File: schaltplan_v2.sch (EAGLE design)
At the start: 18 parts

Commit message: layout/board redesign
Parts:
- removed D10, D3, D4, D5, D6, D7, D8, D9: 1N4004, diode:1N4004
- removed U$3, U$4, U$5: JS_05_MN_KT, n39:JS_05_MN_KT
- removed U$6, U$7, U$8: JS_05_N_K, n39:JS_05_N_K
- added T1, T2: 2N3565, transistor:2N3565
- added X1: SSW-102-02-S-S-RA, con-samtec:SSW-102-02-S-S-RA
- added X3: SSW-103-02-S-S-RA, con-samtec:SSW-103-02-S-S-RA
- added X4: SSW-109-02-S-S-RA, con-samtec:SSW-109-02-S-S-RA
- U$1: value JS_05_N_K -> JS_05_MN_KT; device n39:JS_05_N_K -> n39:JS_05_MN_KT
- U$2: value JS_05_MN_KT -> JS_05_N_K; device n39:JS_05_MN_KT -> n39:JS_05_N_K
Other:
- moved on the sheet: D1, D2
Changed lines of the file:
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@@
 <parts>
 <part name="D1" library="diode" deviceset="1N4004" device=""/>
+<part name="U$1" library="n39" deviceset="JS_05_MN_KT" device=""/>
+<part name="U$2" library="n39" deviceset="JS_05_N_K" device=""/>
+<part name="T1" library="transistor" deviceset="2N3565" device=""/>
+<part name="R1" library="docu-dummy" deviceset="R" device=""/>
 <part name="D2" library="diode" deviceset="1N4004" device=""/>
-<part name="U$1" library="n39" deviceset="JS_05_N_K" device=""/>
-<part name="U$2" library="n39" deviceset="JS_05_MN_KT" device=""/>
-<part name="U$3" library="n39" deviceset="JS_05_MN_KT" device=""/>
-<part name="U$4" library="n39" deviceset="JS_05_MN_KT" device=""/>
-<part name="U$5" library="n39" deviceset="JS_05_MN_KT" device=""/>
-<part name="U$6" library="n39" deviceset="JS_05_N_K" device=""/>
-<part name="U$7" library="n39" deviceset="JS_05_N_K" device=""/>
-<part name="U$8" library="n39" deviceset="JS_05_N_K" device=""/>
-<part name="D3" library="diode" deviceset="1N4004" device=""/>
-<part name="D4" library="diode" deviceset="1N4004" device=""/>
-<part name="D5" library="diode" deviceset="1N4004" device=""/>
-<part name="D6" library="diode" deviceset="1N4004" device=""/>
-<part name="D7" library="diode" deviceset="1N4004" device=""/>
-<part name="D8" library="diode" deviceset="1N4004" device=""/>
-<part name="D9" library="diode" deviceset="1N4004" device=""/>
-<part name="D10" library="diode" deviceset="1N4004" device=""/>
+<part name="T2" library="transistor" deviceset="2N3565" device=""/>
+<part name="R2" library="docu-dummy" deviceset="R" device=""/>
+<part name="X1" library="con-samtec" deviceset="SSW-102-02-S-S" device="-RA"/>
+<part name="X3" library="con-samtec" deviceset="SSW-103-02-S-S" device="-RA"/>
+<part name="X4" library="con-samtec" deviceset="SSW-109-02-S-S" device="-RA"/>
 </parts>
 <sheets>
@@
 </plain>
 <instances>
-<instance part="D1" gate="1" x="38.1" y="58.42" rot="R90"/>
-<instance part="D2" gate="1" x="38.1" y="38.1" rot="R90"/>
-<instance part="U$1" gate="G$1" x="96.52" y="20.32"/>
-<instance part="U$2" gate="G$1" x="53.34" y="48.26"/>
-<instance part="U$3" gate="G$1" x="96.52" y="48.26"/>
-<instance part="U$4" gate="G$1" x="134.62" y="48.26"/>
-<instance part="U$5" gate="G$1" x="134.62" y="30.48"/>
-<instance part="U$6" gate="G$1" x="96.52" y="2.54"/>
-<instance part="U$7" gate="G$1" x="137.16" y="20.32"/>
-<instance part="U$8" gate="G$1" x="137.16" y="2.54"/>
-<instance part="D3" gate="1" x="38.1" y="27.94" rot="R90"/>
-<instance part="D4" gate="1" x="38.1" y="20.32" rot="R90"/>
-<instance part="D5" gate="1" x="33.02" y="27.94" rot="R90"/>
-<instance part="D6" gate="1" x="33.02" y="38.1" rot="R90"/>
-<instance part="D7" gate="1" x="33.02" y="58.42" rot="R90"/>
-<instance part="D8" gate="1" x="22.86" y="30.48" rot="R90"/>
-<instance part="D9" gate="1" x="25.4" y="45.72" rot="R90"/>
-<instance part="D10" gate="1" x="33.02" y="20.32" rot="R90"/>
+<instance part="D1" gate="1" x="71.12" y="53.34"/>
+<instance part="U$1" gate="G$1" x="93.98" y="45.72"/>
+<instance part="U$2" gate="G$1" x="93.98" y="20.32"/>
+<instance part="T1" gate="G$1" x="60.96" y="48.26"/>
+<instance part="R1" gate="G$1" x="50.8" y="48.26"/>
+<instance part="D2" gate="1" x="71.12" y="27.94"/>
+<instance part="T2" gate="G$1" x="60.96" y="22.86"/>
+<instance part="R2" gate="G$1" x="50.8" y="22.86"/>
+<instance part="X1" gate="-1" x="38.1" y="71.12"/>
+<instance part="X1" gate="-2" x="38.1" y="68.58"/>
+<instance part="X3" gate="-1" x="121.92" y="68.58" rot="R180"/>
+<instance part="X3" gate="-2" x="121.92" y="71.12" rot="R180"/>
+<instance part="X3" gate="-3" x="121.92" y="73.66" rot="R180"/>
+<instance part="X4" gate="-1" x="17.78" y="48.26"/>
+<instance part="X4" gate="-2" x="17.78" y="45.72"/>
+<instance part="X4" gate="-3" x="17.78" y="43.18"/>
+<instance part="X4" gate="-4" x="17.78" y="40.64"/>
+<instance part="X4" gate="-5" x="17.78" y="38.1"/>
+<instance part="X4" gate="-6" x="17.78" y="35.56"/>
+<instance part="X4" gate="-7" x="17.78" y="33.02"/>
+<instance part="X4" gate="-8" x="17.78" y="30.48"/>
+<instance part="X4" gate="-9" x="17.78" y="27.94"/>
 </instances>
 <busses>

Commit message: schaltplan_v2 finalized
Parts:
- added C1: (no value), rcl:CPOL-EUE3.5-8
- added C2: (no value), rcl:C-EU025-030X050
- added D10, D3, D4, D5, D6, D7, D8, D9: 1N4004, diode:1N4004
- added R1, R2, R3, R4, R5, R6, R7, R8: (no value), resistor:R-EU_0204/2V
- added T3, T4, T5, T6, T7, T8: 2N3565, transistor:2N3565
- added U$3, U$5, U$7: JS_05_MN_KT, n39:JS_05_MN_KT
- added U$4, U$6, U$8: JS_05_N_K, n39:JS_05_N_K
- added X2: SSW-102-02-S-S-RA, con-samtec:SSW-102-02-S-S-RA
- added X5, X6, X7: SSW-103-02-S-S-RA, con-samtec:SSW-103-02-S-S-RA
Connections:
- new net N$1: X2-1.1, X3-1.1, X5-1.1, X6-1.1, X7-1.1
- new net N$10: C1.-, C2.2, D10.A, T1.C, T2.C, T3.C, T4.C, T5.C, T6.C, T7.C, T8.C, X4-1.1
- new net N$11: R2.1, X4-3.1
- new net N$12: D2.A, T2.E, U$2.P$1
- new net N$13: R6.2, T6.B
- new net N$14: R3.1, X4-4.1
- new net N$16: U$4.P$5, X5-2.1
- new net N$17: U$4.P$4, X5-3.1
- new net N$18: U$3.P$4, U$4.P$3
- new net N$2: U$2.P$5, X3-2.1
- new net N$20: D3.A, T3.E, U$3.P$1
- new net N$21: C1.+, C2.1, D1.C, D2.C, D3.C, D4.C, D5.C, D6.C, D7.C, D8.C, D9.C, U$1.P$2, U$2.P$2, U$3.P$2, U$4.P$2, U$5.P$2, U$6.P$2, U$7.P$2, U$8.P$2
- new net N$22: R3.2, T3.B
- new net N$23: R4.1, X4-5.1
- new net N$25: D4.A, T4.E, U$4.P$1
- new net N$26: R5.1, X4-6.1
- new net N$27: R2.2, T2.B
- new net N$28: R4.2, T4.B
- new net N$3: U$2.P$4, X3-3.1
- new net N$30: U$6.P$5, X6-2.1
- new net N$31: U$6.P$4, X6-3.1
- new net N$32: U$5.P$4, U$6.P$3
- new net N$34: D5.A, T5.E, U$5.P$1
- new net N$36: R5.2, T5.B
- new net N$37: R6.1, X4-7.1
- new net N$39: D6.A, T6.E, U$6.P$1
- new net N$4: U$1.P$4, U$2.P$3
- new net N$40: R8.2, T8.B
- new net N$42: U$8.P$5, X7-2.1
- new net N$43: U$8.P$4, X7-3.1
- new net N$44: U$7.P$4, U$8.P$3
- new net N$46: D7.A, T7.E, U$7.P$1
- new net N$48: R7.2, T7.B
- new net N$49: R7.1, X4-8.1
- new net N$5: U$1.P$3, U$3.P$3, U$5.P$3, U$7.P$3, X2-2.1
- new net N$51: D8.A, T8.E, U$8.P$1
- new net N$53: D9.A, X1-1.1
- new net N$54: D10.C, X1-2.1
- new net N$6: D1.A, T1.E, U$1.P$1
- new net N$7: R8.1, X4-9.1
- new net N$8: R1.2, T1.B
- new net N$9: R1.1, X4-2.1
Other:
- moved on the sheet: X1-1, X1-2, X3-1, X3-2, X3-3

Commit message: more fixes
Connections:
- removed net N$10: C1.-, C2.2, D10.A, T1.C, T2.C, T3.C, T4.C, T5.C, T6.C, T7.C, T8.C, X4-1.1
- removed net N$21: C1.+, C2.1, D1.C, D2.C, D3.C, D4.C, D5.C, D6.C, D7.C, D8.C, D9.C, U$1.P$2, U$2.P$2, U$3.P$2, U$4.P$2, U$5.P$2, U$6.P$2, U$7.P$2, U$8.P$2
- removed net N$53: D9.A, X1-1.1
- removed net N$54: D10.C, X1-2.1
- new net N$15: D9.C, X1-1.1
- new net N$19: D10.A, X1-2.1
- new net N$24: C1.+, C2.2, D10.C, T1.C, T2.C, T3.C, T4.C, T5.C, T6.C, T7.C, T8.C, X4-1.1
- new net N$29: C1.-, C2.1, D1.C, D2.C, D3.C, D4.C, D5.C, D6.C, D7.C, D8.C, D9.A, U$1.P$2, U$2.P$2, U$3.P$2, U$4.P$2, U$5.P$2, U$6.P$2, U$7.P$2, U$8.P$2
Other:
- moved on the sheet: C1, D10, D9

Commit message: more fixes
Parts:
- removed X4: SSW-109-02-S-S-RA, con-samtec:SSW-109-02-S-S-RA
- added X8: SSW-110-02-S-S-RA, con-samtec:SSW-110-02-S-S-RA
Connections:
- removed net N$29 (its old number): C1.-, C2.1, D1.C, D2.C, D3.C, D4.C, D5.C, D6.C, D7.C, D8.C, D9.A, U$1.P$2, U$2.P$2, U$3.P$2, U$4.P$2, U$5.P$2, U$6.P$2, U$7.P$2, U$8.P$2
- new net N$19: C1.-, C2.1, D9.A, T1.C, T2.C, T3.C, T4.C, T5.C, T6.C, T7.C, T8.C, X8-10.1
- net N$11: now also X8-3.1; no longer X4-3.1
- net N$14: now also X8-4.1; no longer X4-4.1
- net N$23: now also X8-5.1; no longer X4-5.1
- net N$24: now also D1.C, D2.C, D3.C, D4.C, D5.C, D6.C, D7.C, D8.C, U$1.P$2, U$2.P$2, U$3.P$2, U$4.P$2, U$5.P$2, U$6.P$2, U$7.P$2, U$8.P$2, X8-1.1; no longer T1.C, T2.C, T3.C, T4.C, T5.C, T6.C, T7.C, T8.C, X4-1.1
- net N$26: now also X8-6.1; no longer X4-6.1
- net N$37: now also X8-7.1; no longer X4-7.1
- net N$49: now also X8-8.1; no longer X4-8.1
- net N$7: now also X8-9.1; no longer X4-9.1
- net N$9: now also X8-2.1; no longer X4-2.1

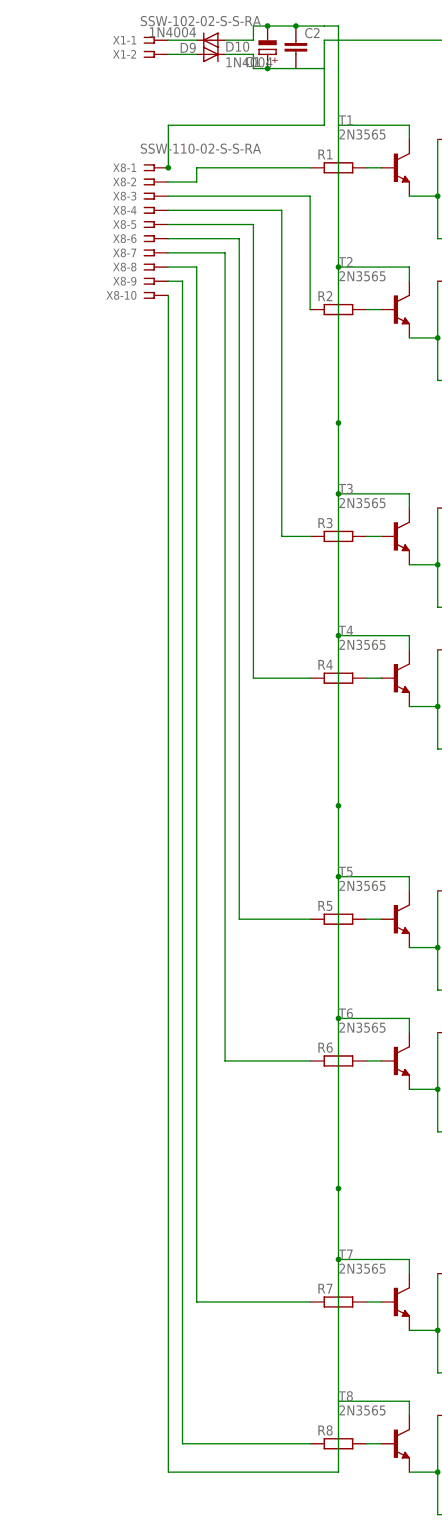
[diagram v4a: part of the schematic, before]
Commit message: change 9pin connector to sub-d
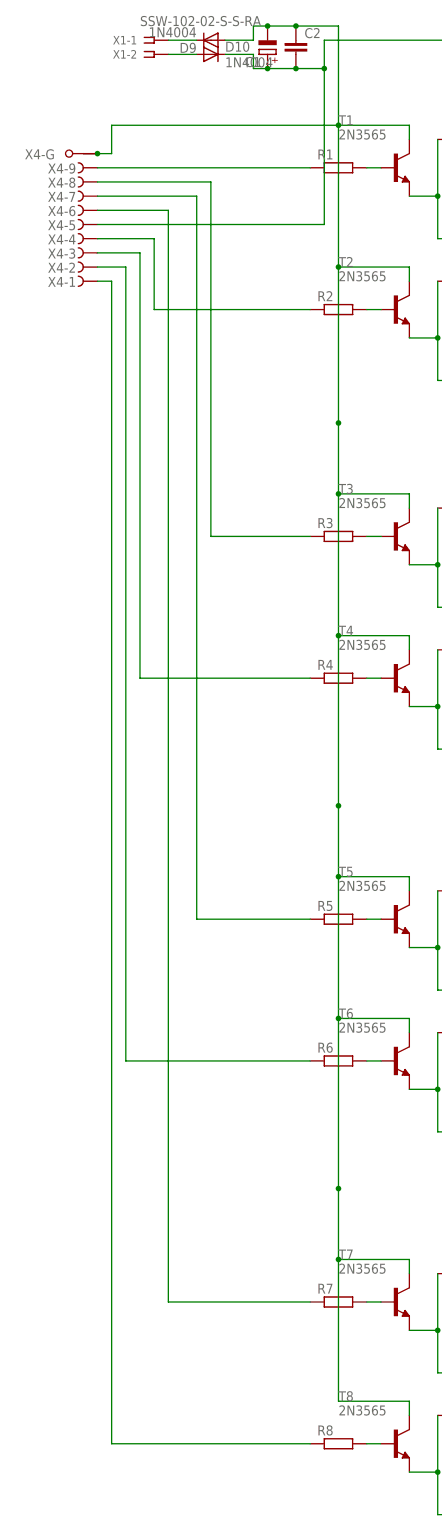
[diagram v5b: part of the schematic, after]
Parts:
- removed X8: SSW-110-02-S-S-RA, con-samtec:SSW-110-02-S-S-RA
- added X4: (no value), con-subd:F09HPS
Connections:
- removed net N$49: R7.1, X8-8.1
- removed net N$7: R8.1, X8-9.1
- removed net N$9: R1.1, X8-2.1
- new net N$15: R8.1, X4-1.F
- new net N$21: R7.1, X4-6.F
- new net N$38: R1.1, X4-9.F
- net N$11: now also R5.1, X4-7.F; no longer R2.1, X8-3.1
- net N$14: now also R6.1, X4-2.F; no longer R3.1, X8-4.1
- net N$19: now also X4-G.G1; no longer X8-10.1
- net N$23: now also X4-3.F; no longer X8-5.1
- net N$24: now also X4-5.F; no longer X8-1.1
- net N$26: now also R2.1, X4-4.F; no longer R5.1, X8-6.1
- net N$37: now also R3.1, X4-8.F; no longer R6.1, X8-7.1

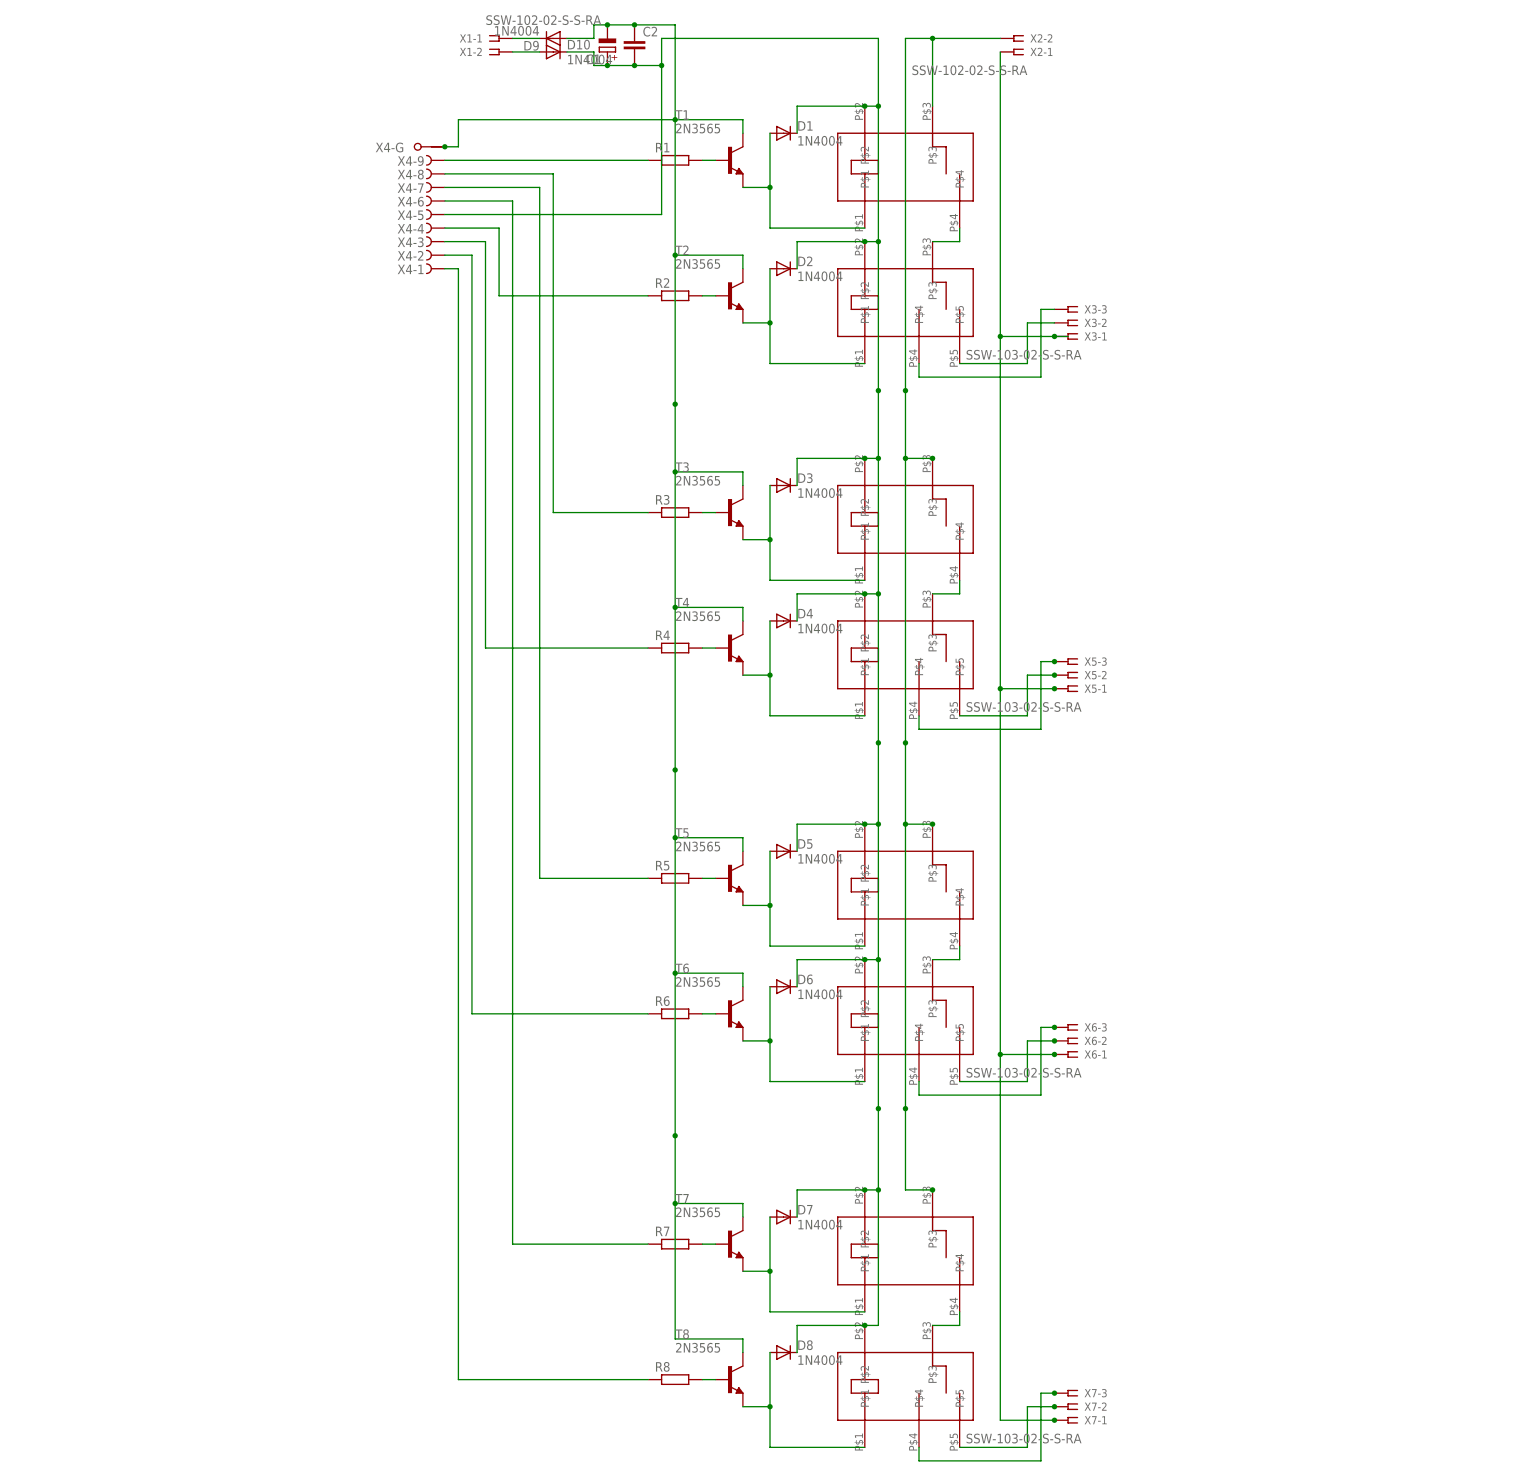
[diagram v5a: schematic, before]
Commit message: added correct connectors
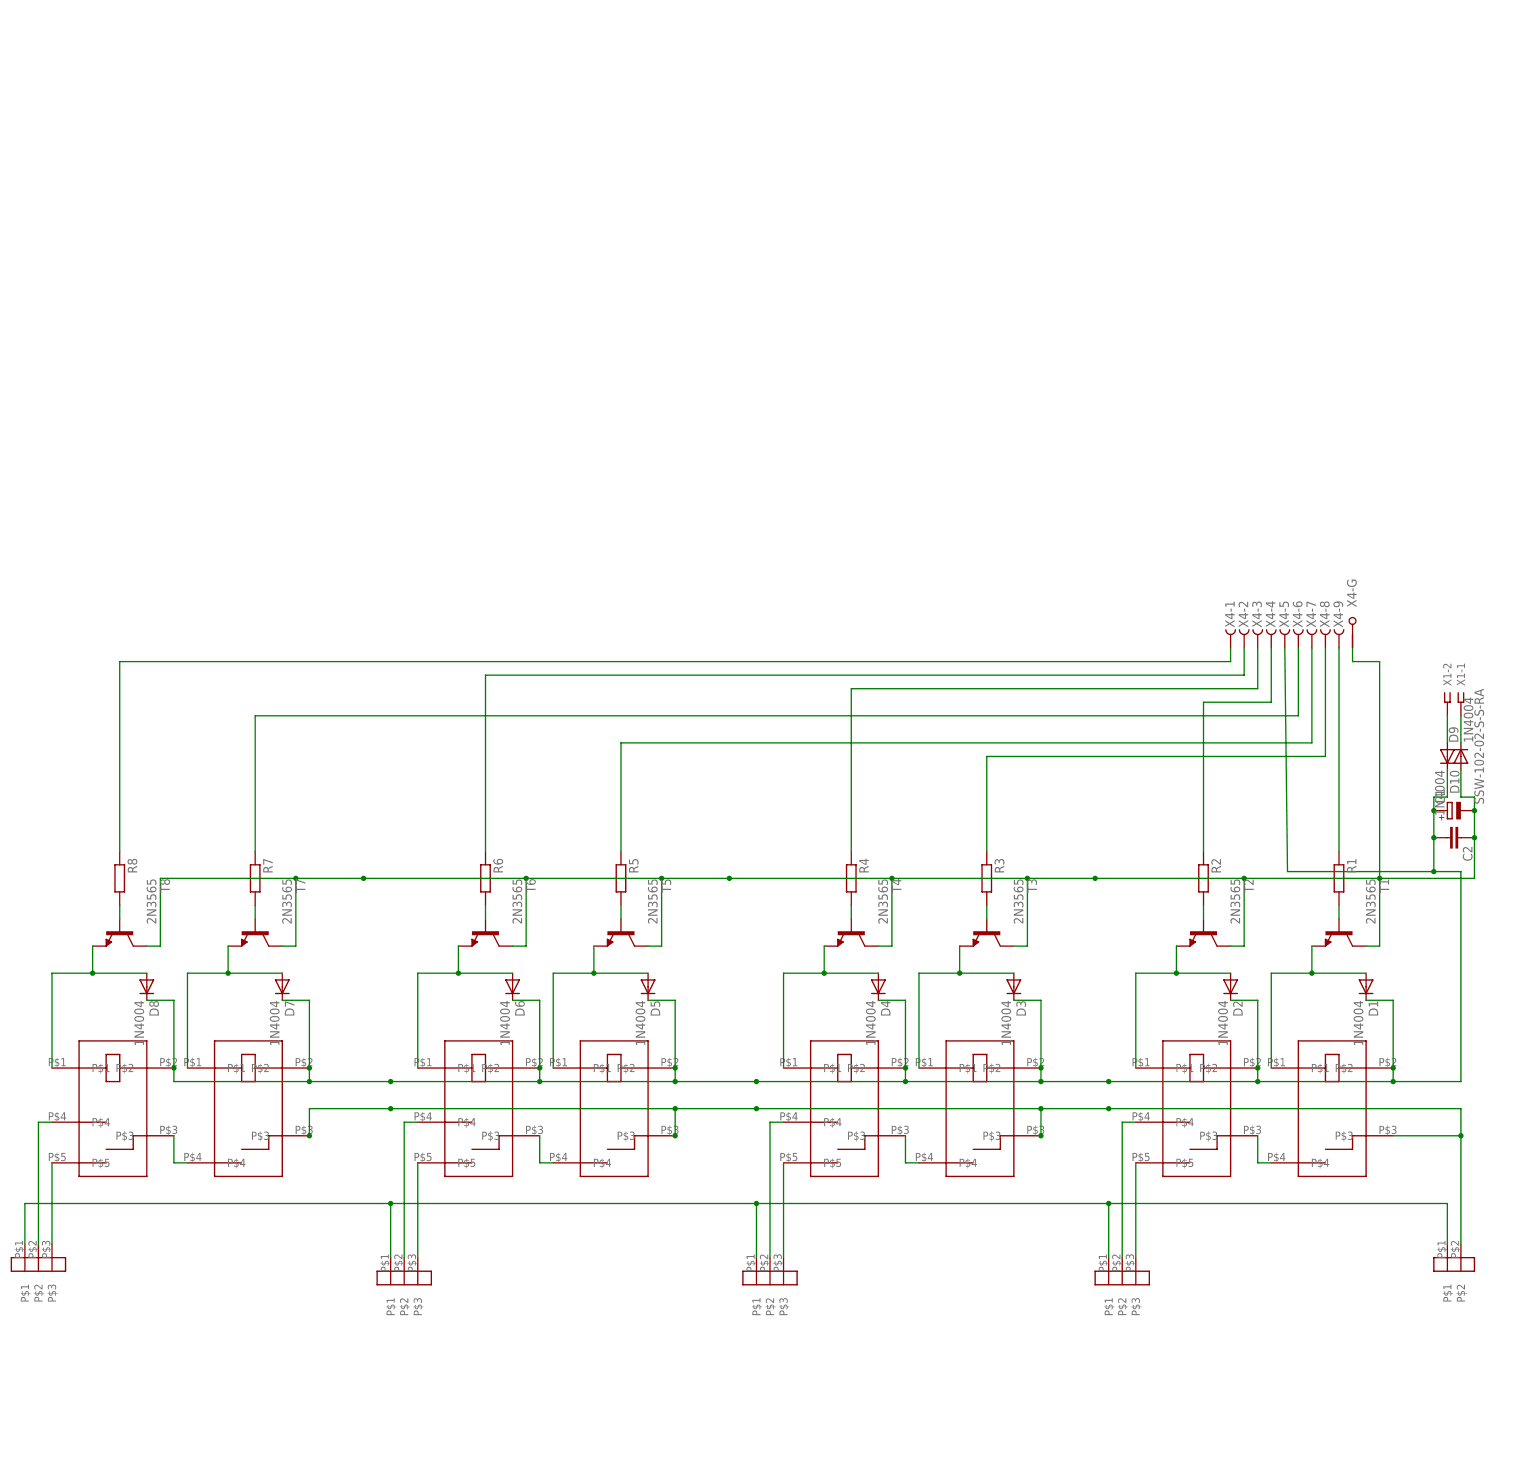
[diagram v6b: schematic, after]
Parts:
- removed X2: SSW-102-02-S-S-RA, con-samtec:SSW-102-02-S-S-RA
- removed X3, X5, X6, X7: SSW-103-02-S-S-RA, con-samtec:SSW-103-02-S-S-RA
- added U$10, U$11, U$12, U$13: WAGO_734_263, n39:WAGO_734_263
- added U$9: WAGO_734_262, n39:WAGO_734_262
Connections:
- net N$1: now also U$10.P$1, U$11.P$1, U$12.P$1, U$13.P$1, U$9.P$1; no longer X2-1.1, X3-1.1, X5-1.1, X6-1.1, X7-1.1
- net N$16: now also U$11.P$3; no longer X5-2.1
- net N$17: now also U$11.P$2; no longer X5-3.1
- net N$2: now also U$10.P$3; no longer X3-2.1
- net N$3: now also U$10.P$2; no longer X3-3.1
- net N$30: now also U$12.P$3; no longer X6-2.1
- net N$31: now also U$12.P$2; no longer X6-3.1
- net N$42: now also U$13.P$3; no longer X7-2.1
- net N$43: now also U$13.P$2; no longer X7-3.1
- net N$5: now also U$9.P$2; no longer X2-2.1
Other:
- moved on the sheet: C1, C2, D1, D10, D2, D3, D4, D5, D6, D7, D8, D9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
